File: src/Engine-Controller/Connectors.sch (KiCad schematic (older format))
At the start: 5 parts, among them P3 SBH11-PBPC-D05-RA-BK, P4 0901471110, P5 66953-005LF, P7 0901471110, U4 SN74LV07ADR

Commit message: Added Ignition System to lib and schematic
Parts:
- removed P3: SBH11-PBPC-D05-RA-BK, Engine-Controller:SBH11-PBPC-D05-RA-BK, symbol Engine-Controller:SBH11-PBPC-D05-RA-BK
- added P3: SBH11-PBPC-D10-RA-BK, Engine-Controller:SBH11-PBPC-D10-RA-BK, symbol Engine-Controller:SBH11-PBPC-D10-RA-BK
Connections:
- net labels added: NRST, SWO
- wire segments 45 -> 65
- no-connect marks 7 -> 6
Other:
- note added: "SWD Programmer\n"
- note removed: "Programmer\n"
- moved on the sheet: P5, P7

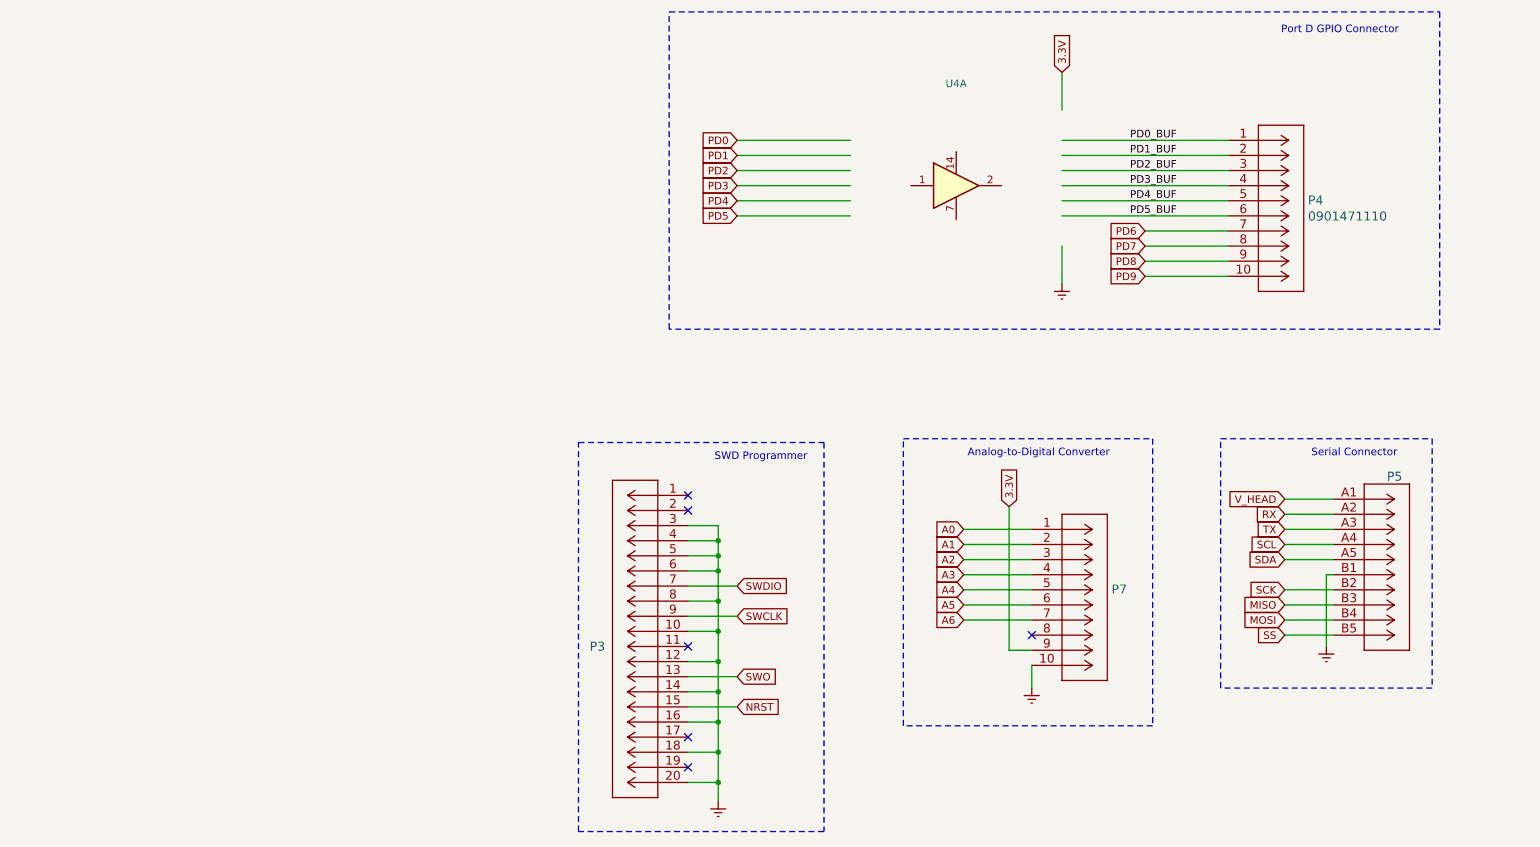
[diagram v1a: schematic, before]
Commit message: Updated Buffer Symbol
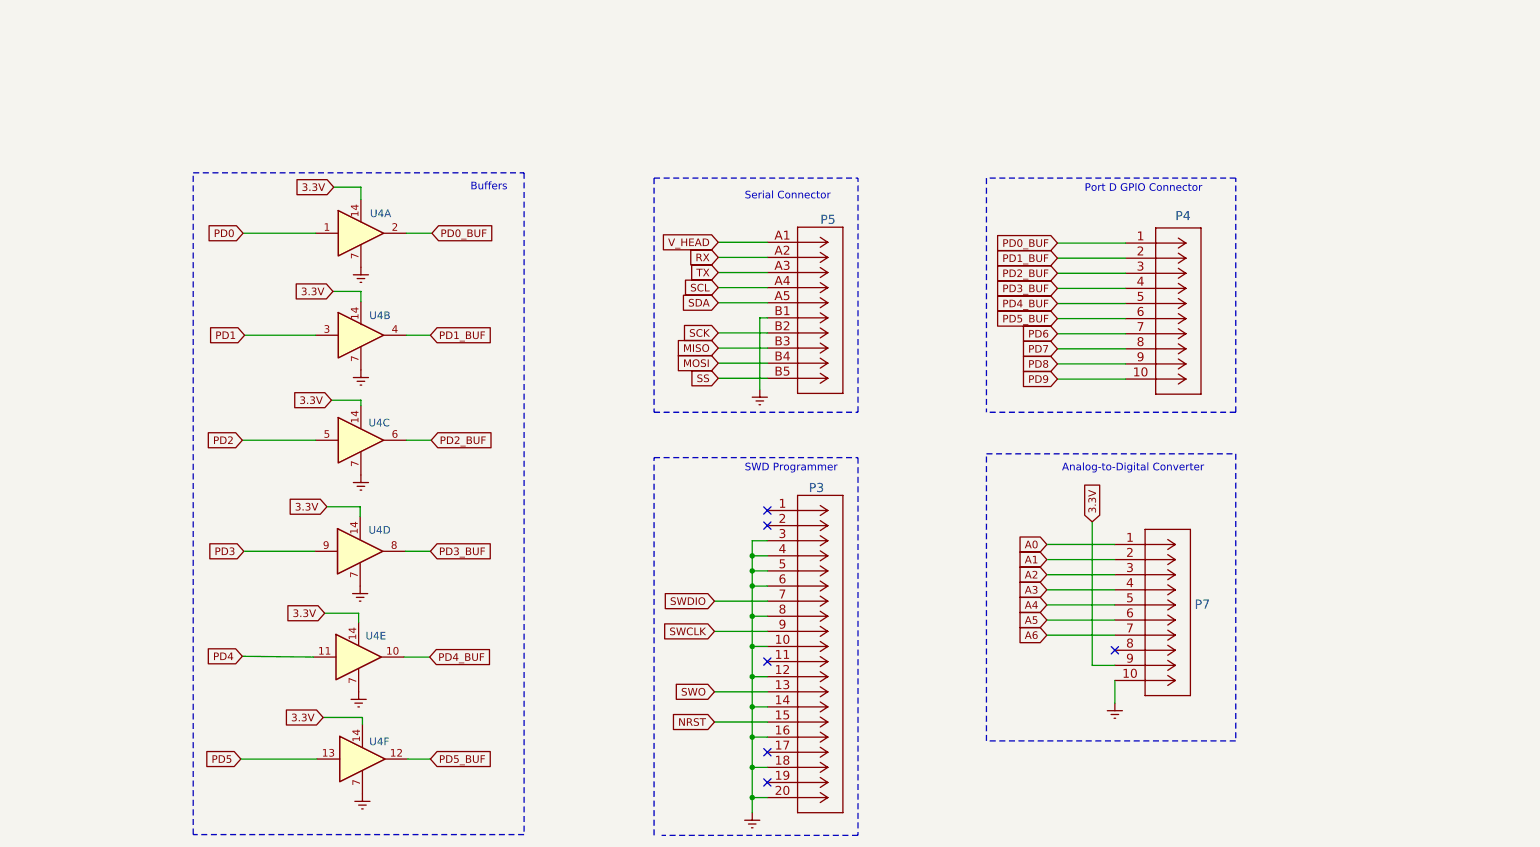
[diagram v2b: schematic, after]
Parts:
- added unit 2 of U4
- added unit 3 of U4
- added unit 4 of U4
- added unit 5 of U4
- added unit 6 of U4
- U4: footprint Engine-Controller:SN74LV07ADR -> (none)
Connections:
- wire segments 65 -> 81
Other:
- note added: "Buffers"
- moved on the sheet: P3, P4, P5, P7

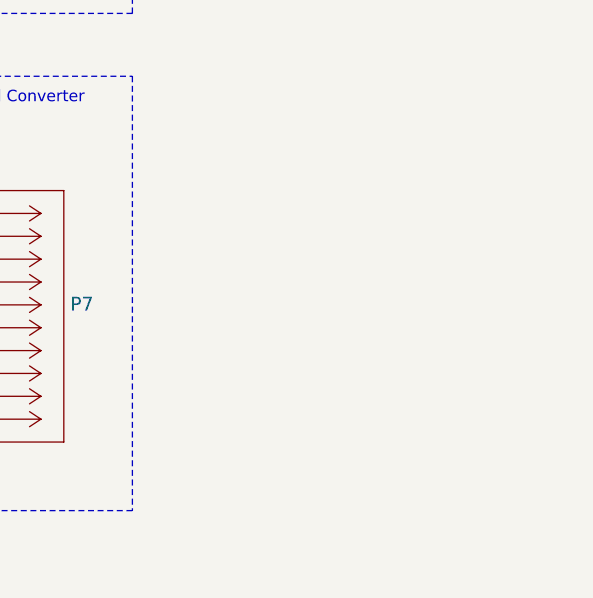
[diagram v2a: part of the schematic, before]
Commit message: Added logo and mounting hole to lib and schematic
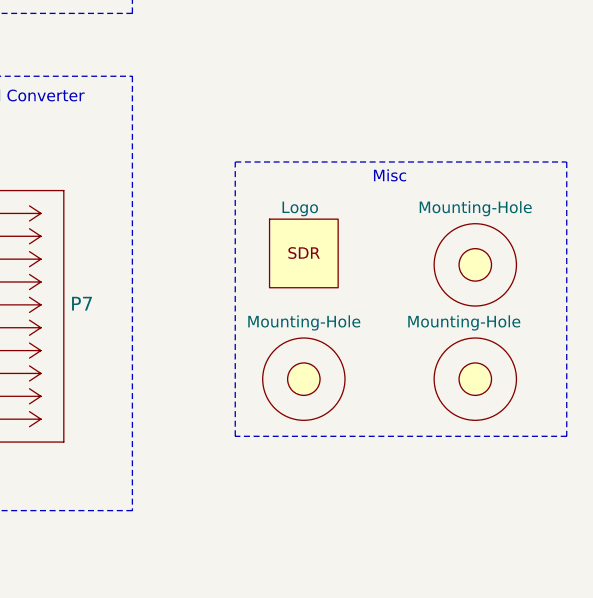
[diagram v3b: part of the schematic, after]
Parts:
- added H? (x3): Mounting-Hole, symbol Engine-Controller:Mounting-Hole
- added LOGO?: Logo, symbol Engine-Controller:Logo
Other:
- note added: "Misc"
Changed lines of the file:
@@
 NoConn ~ 5850 6000
 NoConn ~ 5850 6200
+$Comp
+L Engine-Controller:Logo LOGO?
+U 1 1 618F5F8B
+P 9700 4800
+F 0 "LOGO?" H 9878 4846 50  0001 L CNN
+F 1 "Logo" H 9600 5000 50  0000 L CNN
+F 2 "" H 9700 4800 50  0001 C CNN
+F 3 "" H 9700 4800 50  0001 C CNN
+	1    9700 4800
+	1    0    0    -1
+$EndComp
+$Comp
+L Engine-Controller:Mounting-Hole H?
+U 1 1 618F69A9
+P 9700 5350
+F 0 "H?" H 9908 5396 50  0001 L CNN
+F 1 "Mounting-Hole" H 9450 5600 50  0000 L CNN
+F 2 "" H 9700 5350 50  0001 C CNN
+F 3 "" H 9700 5350 50  0001 C CNN
+	1    9700 5350
+	1    0    0    -1
+$EndComp
+$Comp
+L Engine-Controller:Mounting-Hole H?
+U 1 1 618F7698
+P 10450 4850
+F 0 "H?" H 10658 4896 50  0001 L CNN
+F 1 "Mounting-Hole" H 10200 5100 50  0000 L CNN
+F 2 "" H 10450 4850 50  0001 C CNN
+F 3 "" H 10450 4850 50  0001 C CNN
+	1    10450 4850
+	1    0    0    -1
+$EndComp
+$Comp
+L Engine-Controller:Mounting-Hole H?
+U 1 1 618F7988
+P 10450 5350
+F 0 "H?" H 10658 5396 50  0001 L CNN
+F 1 "Mounting-Hole" H 10150 5600 50  0000 L CNN
+F 2 "" H 10450 5350 50  0001 C CNN
+F 3 "" H 10450 5350 50  0001 C CNN
+	1    10450 5350
+	1    0    0    -1
+$EndComp
+Wire Notes Line
+	10850 4400 10850 5600
+Wire Notes Line
+	10850 5600 9400 5600
+Wire Notes Line
+	9400 5600 9400 4400
+Wire Notes Line
+	9400 4400 10850 4400
+Text Notes 10000 4500 0    50   ~ 0
+Misc
 $EndSCHEMATC

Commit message: finished routing rev3.0
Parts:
- H1, H2, H3: renamed from H?; footprint (none) -> Engine-Controller:MountingHole_4.3mm_M4_DIN965
- LOGO1: renamed from LOGO?; footprint (none) -> Engine-Controller:Logo
- U4: footprint (none) -> Engine-Controller:SN74LV07ADR
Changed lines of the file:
@@
 F 0 "U4" H 3220 2695 50  0000 L CNN
 F 1 "SN74LV07ADR" H 2970 2325 50  0001 C CNN
-F 2 "" H 3160 2565 50  0001 C CNN
+F 2 "Engine-Controller:SN74LV07ADR" H 3160 2565 50  0001 C CNN
 F 3 "http://www.ti.com/lit/ds/symlink/cd4010b-q1.pdf" H 3160 2565 50  0001 C CNN
 	1    3160 2565
@@
 F 0 "U4" H 3215 3370 50  0000 L CNN
 F 1 "SN74LV07ADR" H 2970 3000 50  0001 C CNN
-F 2 "" H 3160 3240 50  0001 C CNN
+F 2 "Engine-Controller:SN74LV07ADR" H 3160 3240 50  0001 C CNN
 F 3 "http://www.ti.com/lit/ds/symlink/cd4010b-q1.pdf" H 3160 3240 50  0001 C CNN
 	2    3160 3240
@@
 F 0 "U4" H 3210 4050 50  0000 L CNN
 F 1 "SN74LV07ADR" H 2970 3695 50  0001 C CNN
-F 2 "" H 3160 3935 50  0001 C CNN
+F 2 "Engine-Controller:SN74LV07ADR" H 3160 3935 50  0001 C CNN
 F 3 "http://www.ti.com/lit/ds/symlink/cd4010b-q1.pdf" H 3160 3935 50  0001 C CNN
 	3    3160 3935
@@
 F 0 "U4" H 3210 4810 50  0000 L CNN
 F 1 "SN74LV07ADR" H 2965 4430 50  0001 C CNN
-F 2 "" H 3155 4670 50  0001 C CNN
+F 2 "Engine-Controller:SN74LV07ADR" H 3155 4670 50  0001 C CNN
 F 3 "http://www.ti.com/lit/ds/symlink/cd4010b-q1.pdf" H 3155 4670 50  0001 C CNN
 	4    3155 4670
@@
 F 0 "U4" H 3190 5510 50  0000 L CNN
 F 1 "SN74LV07ADR" H 2955 5130 50  0001 C CNN
-F 2 "" H 3145 5370 50  0001 C CNN
+F 2 "Engine-Controller:SN74LV07ADR" H 3145 5370 50  0001 C CNN
 F 3 "http://www.ti.com/lit/ds/symlink/cd4010b-q1.pdf" H 3145 5370 50  0001 C CNN
 	5    3145 5370
@@
 F 0 "U4" H 3215 6160 50  0000 L CNN
 F 1 "SN74LV07ADR" H 2980 5805 50  0001 C CNN
-F 2 "" H 3170 6045 50  0001 C CNN
+F 2 "Engine-Controller:SN74LV07ADR" H 3170 6045 50  0001 C CNN
 F 3 "http://www.ti.com/lit/ds/symlink/cd4010b-q1.pdf" H 3170 6045 50  0001 C CNN
 	6    3170 6045
@@
 NoConn ~ 5850 6200
 $Comp
-L Engine-Controller:Logo LOGO?
+L Engine-Controller:Logo LOGO1
 U 1 1 618F5F8B
 P 9700 4800
-F 0 "LOGO?" H 9878 4846 50  0001 L CNN
+F 0 "LOGO1" H 9878 4846 50  0001 L CNN
 F 1 "Logo" H 9600 5000 50  0000 L CNN
-F 2 "" H 9700 4800 50  0001 C CNN
+F 2 "Engine-Controller:Logo" H 9700 4800 50  0001 C CNN
 F 3 "" H 9700 4800 50  0001 C CNN
 	1    9700 4800
@@
 $EndComp
 $Comp
-L Engine-Controller:Mounting-Hole H?
+L Engine-Controller:Mounting-Hole H1
 U 1 1 618F69A9
 P 9700 5350
-F 0 "H?" H 9908 5396 50  0001 L CNN
+F 0 "H1" H 9908 5396 50  0001 L CNN
 F 1 "Mounting-Hole" H 9450 5600 50  0000 L CNN
-F 2 "" H 9700 5350 50  0001 C CNN
+F 2 "Engine-Controller:MountingHole_4.3mm_M4_DIN965" H 9700 5350 50  0001 C CNN
 F 3 "" H 9700 5350 50  0001 C CNN
 	1    9700 5350
@@
 $EndComp
 $Comp
-L Engine-Controller:Mounting-Hole H?
+L Engine-Controller:Mounting-Hole H2
 U 1 1 618F7698
 P 10450 4850
-F 0 "H?" H 10658 4896 50  0001 L CNN
+F 0 "H2" H 10658 4896 50  0001 L CNN
 F 1 "Mounting-Hole" H 10200 5100 50  0000 L CNN
-F 2 "" H 10450 4850 50  0001 C CNN
+F 2 "Engine-Controller:MountingHole_4.3mm_M4_DIN965" H 10450 4850 50  0001 C CNN
 F 3 "" H 10450 4850 50  0001 C CNN
 	1    10450 4850
@@
 $EndComp
 $Comp
-L Engine-Controller:Mounting-Hole H?
+L Engine-Controller:Mounting-Hole H3
 U 1 1 618F7988
 P 10450 5350
-F 0 "H?" H 10658 5396 50  0001 L CNN
+F 0 "H3" H 10658 5396 50  0001 L CNN
 F 1 "Mounting-Hole" H 10150 5600 50  0000 L CNN
-F 2 "" H 10450 5350 50  0001 C CNN
+F 2 "Engine-Controller:MountingHole_4.3mm_M4_DIN965" H 10450 5350 50  0001 C CNN
 F 3 "" H 10450 5350 50  0001 C CNN
 	1    10450 5350
